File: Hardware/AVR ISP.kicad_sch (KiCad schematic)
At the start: 16 parts, among them IC1 ATMEGA328, IC2 ATTINY2313, IC3 ATTINY85, Y1 Crystal

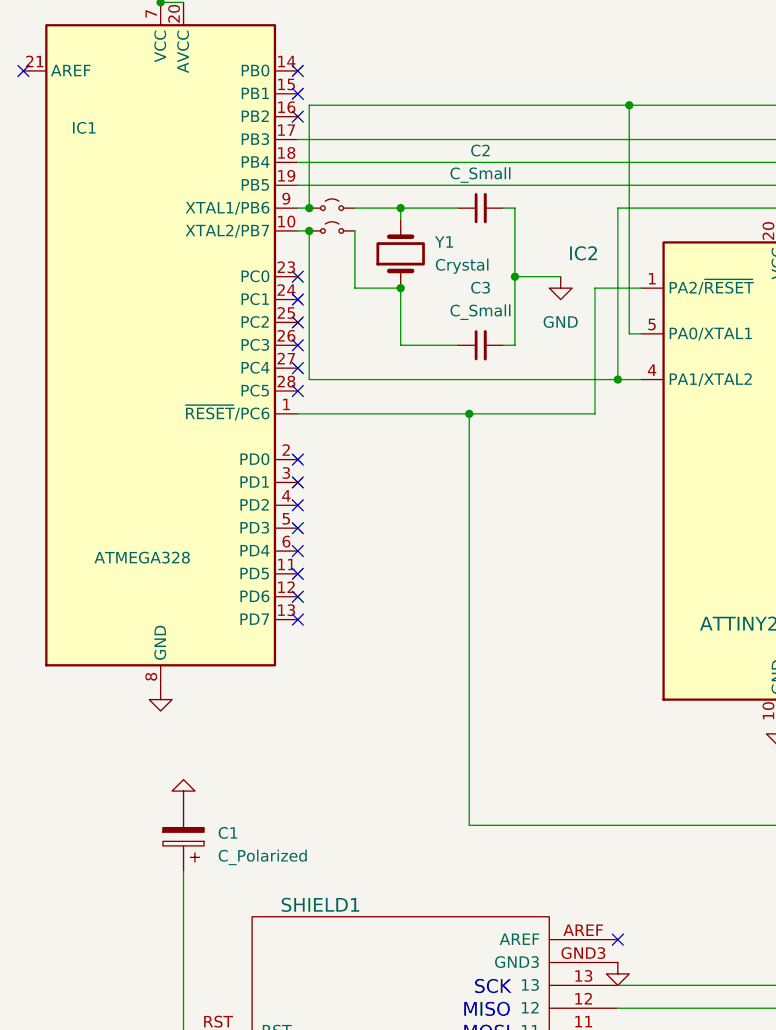
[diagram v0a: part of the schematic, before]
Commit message: Updated PCB and images
Updated PCB removing plating around the four sheild holes
Added an image of the built PCB

Signed-off-by: Robert Knutsson <zybreak@gmail.com>
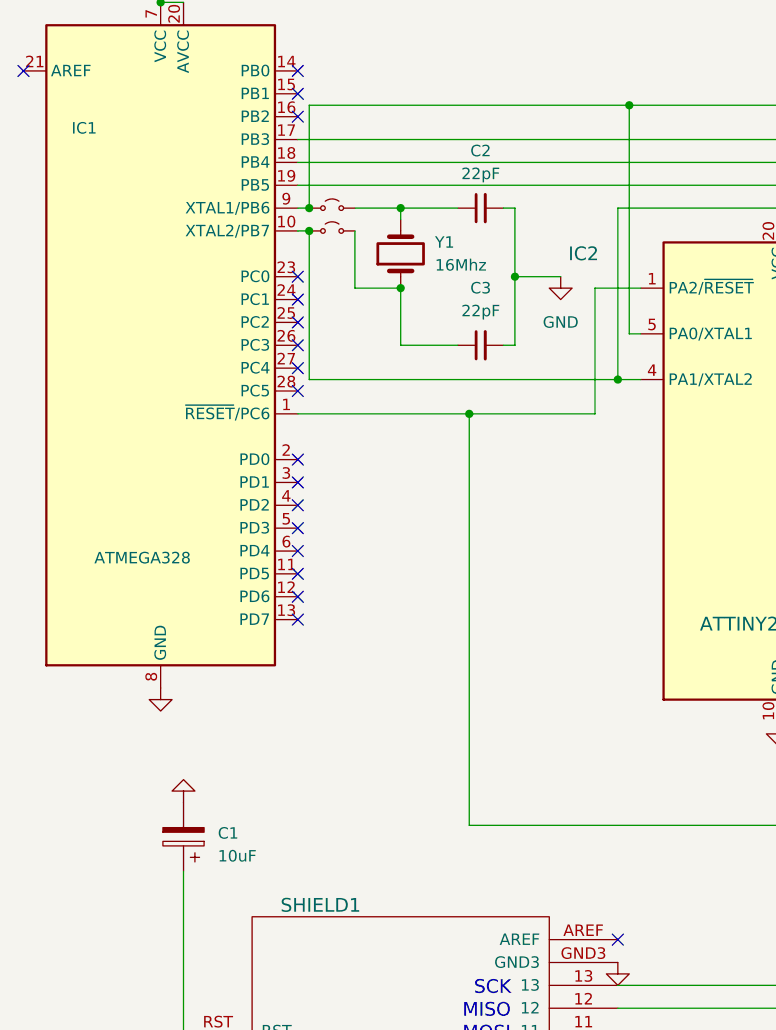
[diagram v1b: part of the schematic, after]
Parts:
- C1: value C_Polarized -> 10uF
- C2, C3: value C_Small -> 22pF
- Y1: value Crystal -> 16Mhz
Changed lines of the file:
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@@
 			)
 		)
-		(property "Value" "C_Small"
+		(property "Value" "22pF"
 			(at 74.9363 38.1 90)
 			(show_name no)
@@
 			)
 		)
-		(property "Value" "C_Polarized"
+		(property "Value" "10uF"
 			(at 45.72 113.9189 0)
 			(show_name no)
@@
 			)
 		)
-		(property "Value" "C_Small"
+		(property "Value" "22pF"
 			(at 74.9363 53.34 90)
 			(show_name no)
@@
 			)
 		)
-		(property "Value" "Crystal"
+		(property "Value" "16Mhz"
 			(at 69.85 48.2599 90)
 			(show_name no)
